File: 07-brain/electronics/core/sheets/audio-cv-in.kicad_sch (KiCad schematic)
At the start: 20 parts, among them Q3 BC847BS, U2 TL072

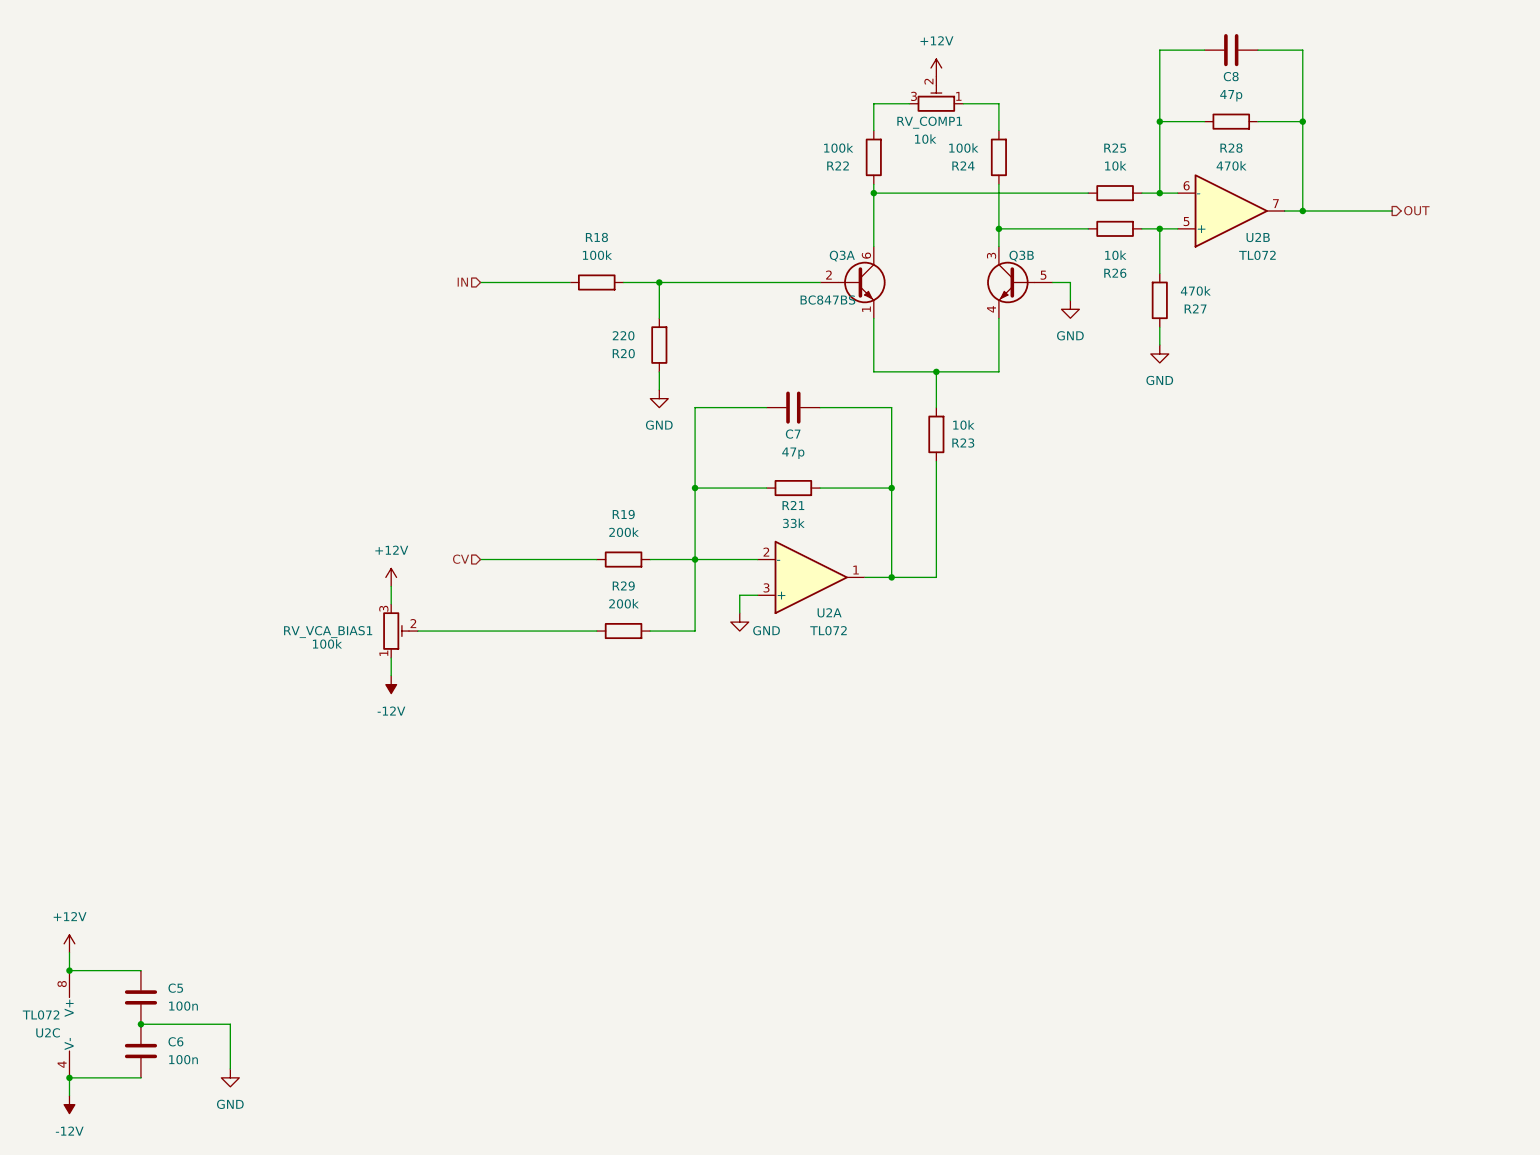
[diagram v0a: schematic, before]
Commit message: ADSR + VCA v0.2
- The + and - power pins on the VCA op-amp was accidentally swapped. This version fixes it
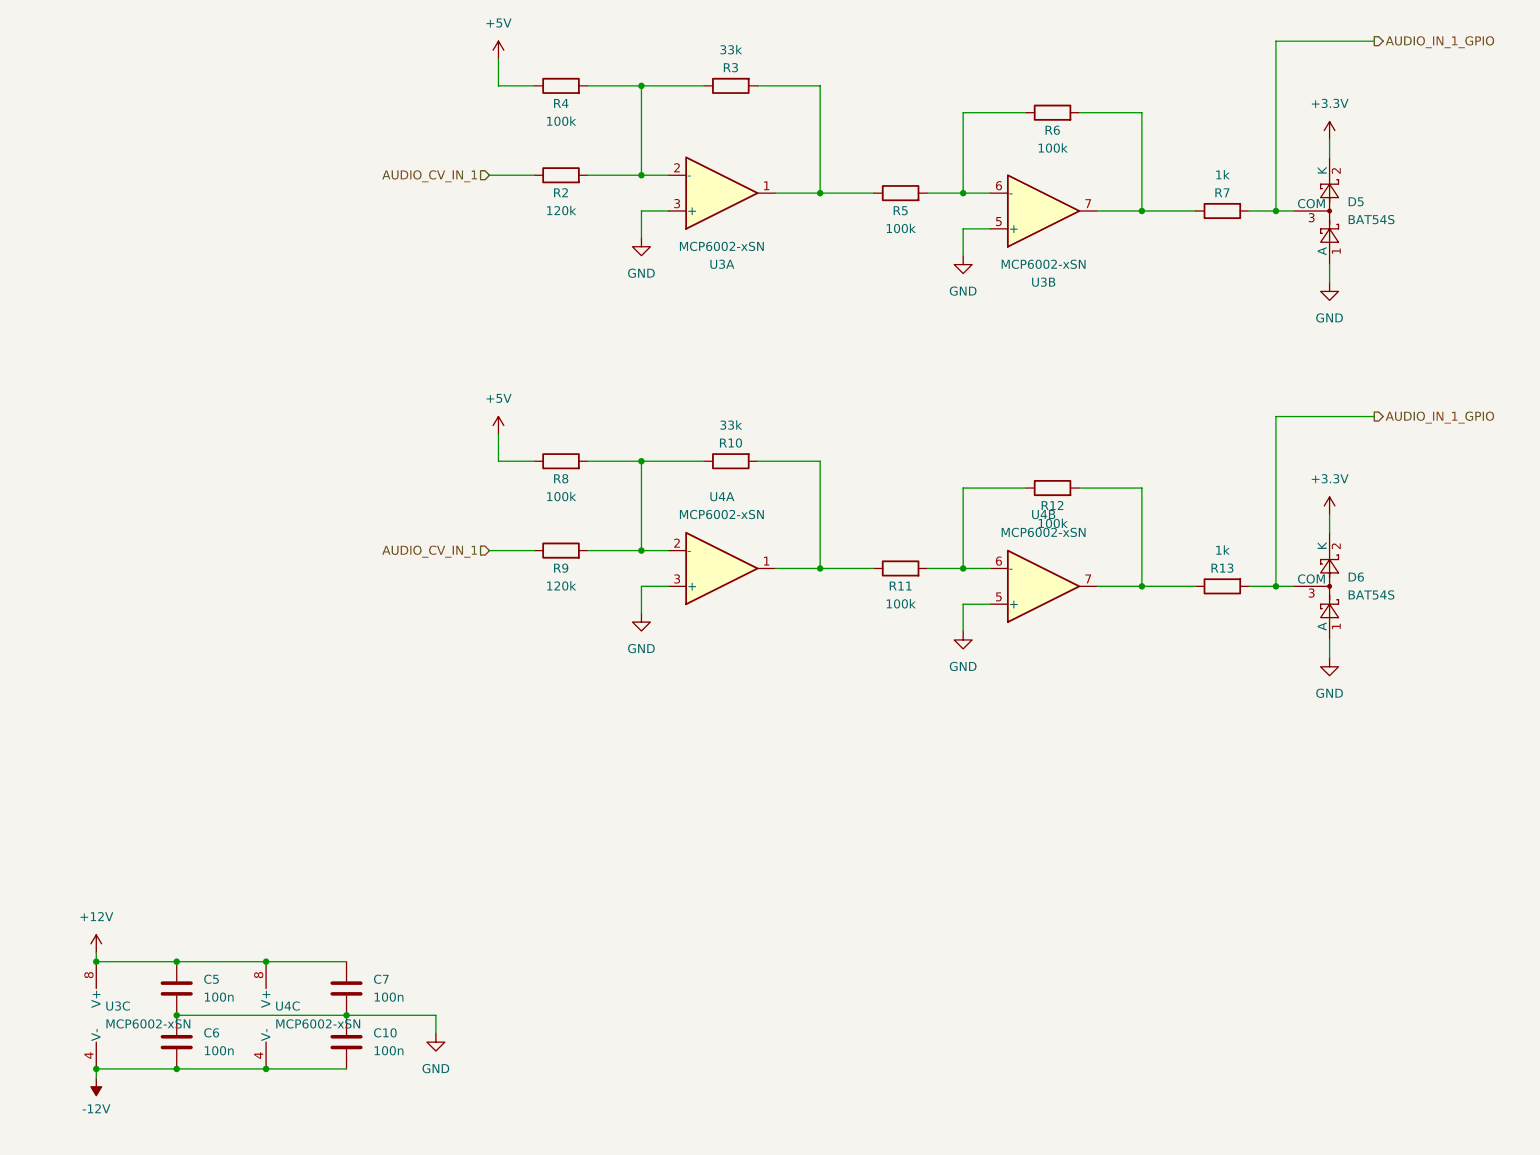
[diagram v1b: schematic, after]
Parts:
- removed C8: 47p, Capacitor_SMD:C_0603_1608Metric_Pad1.08x0.95mm_HandSolder, symbol Device:C
- removed Q3: BC847BS, Package_TO_SOT_SMD:SOT-363_SC-70-6, symbol Transistor_BJT:BC847BS
- removed R18, R22, R24: 100k, Resistor_SMD:R_0603_1608Metric, symbol Device:R
- removed R19, R29: 200k, Resistor_SMD:R_0603_1608Metric, symbol Device:R
- removed R20: 220, Resistor_SMD:R_0603_1608Metric, symbol Device:R
- removed R21: 33k, Resistor_SMD:R_0603_1608Metric, symbol Device:R
- removed R23, R25, R26: 10k, Resistor_SMD:R_0603_1608Metric, symbol Device:R
- removed R27, R28: 470k, Resistor_SMD:R_0603_1608Metric, symbol Device:R
- removed RV_COMP1: 10k, Potentiometer_THT:Potentiometer_ACP_CA6-H2,5_Horizontal, symbol Device:R_Potentiometer_Trim
- removed RV_VCA_BIAS1: 100k, Potentiometer_THT:Potentiometer_ACP_CA6-H2,5_Horizontal, symbol Device:R_Potentiometer_Trim
- removed U2: TL072, Package_SO:SOIC-8_3.9x4.9mm_P1.27mm, symbol Amplifier_Operational:TL072
- added C10: 100n, Capacitor_SMD:C_0603_1608Metric, symbol Device:C
- added D5, D6: BAT54S, Package_TO_SOT_SMD:SOT-23, symbol Diode:BAT54S
- added R10, R3: 33k, Resistor_SMD:R_0603_1608Metric, symbol Device:R
- added R11, R12, R4, R5, R6, R8: 100k, Resistor_SMD:R_0603_1608Metric, symbol Device:R
- added R13, R7: 1k, Resistor_SMD:R_0603_1608Metric, symbol Device:R
- added R2, R9: 120k, Resistor_SMD:R_0603_1608Metric, symbol Device:R
- added U3, U4: MCP6002-xSN, symbol Amplifier_Operational:MCP6002-xSN
- C5, C6: CHECKED YES -> (none)
- C7: value 47p -> 100n; footprint Capacitor_SMD:C_0603_1608Metric_Pad1.08x0.95mm_HandSolder -> Capacitor_SMD:C_0603_1608Metric; CHECKED YES -> (none); LCSC C1671 -> C14663
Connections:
- net +12V: now also C7.1, U3.8 (V+), U4.8 (V+)
- net -12V: now also C10.2, U3.4 (V-), U4.4 (V-)
- net GND: now also C7.2, C10.1, D5.1 (A), D6.1 (A), U3.3 (+), U3.5 (+), U4.3 (+), U4.5 (+)
- new net: R3.2, R5.1, U3.1
- new net: R5.2, R6.1, U3.6 (-)
- new net: R6.2, R7.1, U3.7
- new net: R12.2, R13.1, U4.7
- new net: R10.2, R11.1, U4.1
- new net: R10.1, R8.2, R9.2, U4.2 (-)
- new net: R2.2, R3.1, R4.2, U3.2 (-)
- new net: R11.2, R12.1, U4.6 (-)
- new net +3.3V: D5.2 (K), D6.2 (K)
- new net +5V: R4.1, R8.1
- new net AUDIO_CV_IN_1: R2.1, R9.1
- new net AUDIO_IN_1_GPIO: D5.3 (COM), D6.3 (COM), R13.2, R7.2

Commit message: Added MIDI input circuit
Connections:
- net AUDIO_CV_IN_1: no longer R9.1
- net AUDIO_IN_1_GPIO: no longer D6.3 (COM), R13.2
- new net AUDIO_CV_IN_2: R9.1
- new net AUDIO_IN_2_GPIO: D6.3 (COM), R13.2
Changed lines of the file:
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@@
 		)
 	)
-	(hierarchical_label "AUDIO_CV_IN_1"
+	(hierarchical_label "AUDIO_CV_IN_2"
 		(shape input)
 		(at 82.55 109.22 180)
@@
 		)
 	)
-	(hierarchical_label "AUDIO_IN_1_GPIO"
+	(hierarchical_label "AUDIO_IN_2_GPIO"
 		(shape output)
 		(at 208.28 90.17 0)
@@
 		(on_board yes)
 		(dnp no)
-		(fields_autoplaced yes)
 		(property "Reference" "U4"
 			(at 115.57 101.6 0)
@@
 		(on_board yes)
 		(dnp no)
-		(fields_autoplaced yes)
 		(property "Reference" "U4"
-			(at 161.29 104.14 0)
+			(at 165.1 118.11 0)
 			(effects
 				(font
@@
 		)
 		(property "Value" "MCP6002-xSN"
-			(at 161.29 106.68 0)
-			(effects
-				(font
+			(at 165.1 120.65 0)
+			(effects
+				(font

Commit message: Added audio io to Brain
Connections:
- net AUDIO_IN_1_GPIO renamed GPIO_AUDIO_IN_1
- net AUDIO_IN_2_GPIO renamed GPIO_AUDIO_IN_2
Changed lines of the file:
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@@
 		)
 	)
-	(hierarchical_label "AUDIO_IN_2_GPIO"
+	(hierarchical_label "GPIO_AUDIO_IN_2"
 		(shape output)
 		(at 208.28 90.17 0)
@@
 		)
 	)
-	(hierarchical_label "AUDIO_IN_1_GPIO"
+	(hierarchical_label "GPIO_AUDIO_IN_1"
 		(shape output)
 		(at 208.28 36.83 0)

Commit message: Brain schematics WIP
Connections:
- net GND renamed GNDA

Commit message: Audio/CV out BrainSDK tested/working
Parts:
- removed U3, U4: MCP6002-xSN, symbol Amplifier_Operational:MCP6002-xSN
- added U8, U9: TL072, symbol Amplifier_Operational:TL072
- renumbered C5 to C12, C6 to C13, C7 to C14, C10 to C15, R4 to R24, R2 to R25, R8 to R26, R9 to R27, R3 to R28, R10 to R29, R5 to R30, R11 to R31, R6 to R32, R12 to R33, R7 to R34, R13 to R35
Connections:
- net +12V: now also U8.8 (V+), U9.8 (V+)
- net -12V: now also U8.4 (V-), U9.4 (V-)
- net GNDA: now also U8.3 (+), U8.5 (+), U9.3 (+), U9.5 (+); no longer C12.2, C13.1
- net at R28.2, R30.1: now also U8.1
- net at R30.2, R32.1: now also U8.6 (-)
- net at R32.2, R34.1: now also U8.7
- net at R33.2, R35.1: now also U9.7
- net at R29.2, R31.1: now also U9.1
- net at R26.2, R27.2, R29.1: now also U9.2 (-)
- net at R24.2, R25.2, R28.1: now also U8.2 (-)
- net at R31.2, R33.1: now also U9.6 (-)
- new net: C12.2, C13.1
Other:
- moved on the sheet: C12, C13

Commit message: Design Brain/Core PCB
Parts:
- U8, U9: footprint (none) -> Package_SO:SOIC-8_3.9x4.9mm_P1.27mm
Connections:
- net GNDA: now also C12.2, C13.1
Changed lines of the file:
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@@
 	)
 	(junction
+		(at 50.8 175.26)
+		(diameter 0)
+		(color 0 0 0 0)
+	)
+	(junction
 		(at 104.14 43.18)
 		(diameter 0)
@@
 	(wire
 		(pts
+			(xy 50.8 175.26) (xy 62.23 175.26)
+		)
+		(stroke
+			(width 0)
+			(type default)
+		)
+	)
+	(wire
+		(pts
 			(xy 175.26 60.96) (xy 182.88 60.96)
 		)
@@
 			)
 		)
-		(property "Footprint" ""
+		(property "Footprint" "Package_SO:SOIC-8_3.9x4.9mm_P1.27mm"
 			(at 43.18 175.26 0)
 			(effects
@@
 			)
 		)
-		(property "Footprint" ""
+		(property "Footprint" "Package_SO:SOIC-8_3.9x4.9mm_P1.27mm"
 			(at 161.29 60.96 0)
 			(effects
@@
 			)
 		)
-		(property "Footprint" ""
+		(property "Footprint" "Package_SO:SOIC-8_3.9x4.9mm_P1.27mm"
 			(at 29.21 175.26 0)
 			(effects
@@
 			)
 		)
-		(property "Footprint" ""
+		(property "Footprint" "Package_SO:SOIC-8_3.9x4.9mm_P1.27mm"
 			(at 161.29 114.3 0)
 			(effects
@@
 			)
 		)
-		(property "Footprint" ""
+		(property "Footprint" "Package_SO:SOIC-8_3.9x4.9mm_P1.27mm"
 			(at 115.57 58.42 0)
 			(effects
@@
 			)
 		)
-		(property "Footprint" ""
+		(property "Footprint" "Package_SO:SOIC-8_3.9x4.9mm_P1.27mm"
 			(at 115.57 111.76 0)
 			(effects

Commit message: Brain PCB WIP
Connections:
- net GNDA renamed GND
